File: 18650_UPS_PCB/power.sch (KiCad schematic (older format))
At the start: 37 parts, among them SW1 ENABLE, SW5 ENABLE, U2 R5478, U3 STC4054, U4 FS8205A, U5 TPS63000, U6 TPS63000

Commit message: layout almost done
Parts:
- removed JP1, JP2: PWRSAVE, Jumper:SolderJumper-3_P1.3mm_Open_RoundedPad1.0x1.5mm, symbol Jumper:SolderJumper_3_Open
- removed SW5: ENABLE, Button_Switch_THT:SW_CuK_OS102011MA1QN1_SPDT_Angled, symbol Switch:SW_SPDT
- BT1: footprint CUSTOM_FOOTPRINTS:Keystone_1042 -> Battery:BatteryHolder_Keystone_1042_1x18650
- SW1: value ENABLE -> SW_SPDT; footprint Button_Switch_THT:SW_CuK_OS102011MA1QN1_SPDT_Angled -> CUSTOM_FOOTPRINTS:ALPS_SPEF210101
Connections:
- net GNDD: no longer SW1.3 (C)
- net Shunt+: now also SW1.3 (C); no longer BT1.1 (+)
- net at U5.6 (EN): now also C6.2, R6.2, U5.8 (VINA); no longer SW1.2 (B)
- net PA4: now reaches U5.7 (PS/SYNC)
- net PA5: now reaches U6.7 (PS/SYNC)
- net at U6.6 (EN): now also C7.2, R7.2, U6.8 (VINA)
- new net: BT1.1 (+), SW1.2 (B)
- now unconnected: SW1.1 (A)
- no-connect marks 0 -> 1
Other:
- moved on the sheet: BT1
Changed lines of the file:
@@
 $Descr A4 11693 8268
 encoding utf-8
-Sheet 2 4
+Sheet 2 2
 Title ""
 Date ""
@@
 	4700 2100 4700 2200
 Connection ~ 5250 1500
-$Comp
-L Switch:SW_SPDT SW?
-U 1 1 6096E9F7
-P 5700 2000
-AR Path="/6096E9F7" Ref="SW?"  Part="1"
-AR Path="/60952D5B/6096E9F7" Ref="SW1"  Part="1"
-F 0 "SW1" H 5700 1800 50  0000 C CNN
-F 1 "ENABLE" H 5700 1700 50  0000 C CNN
-F 2 "Button_Switch_THT:SW_CuK_OS102011MA1QN1_SPDT_Angled" H 5700 2000 50  0001 C CNN
-F 3 "~" H 5700 2000 50  0001 C CNN
-	1    5700 2000
-	-1   0    0    -1
-$EndComp
-Wire Wire Line
-	5500 2100 5250 2100
-Connection ~ 5250 2100
-Wire Wire Line
-	5500 1900 5450 1900
-Wire Wire Line
-	5900 2000 5950 2000
-Wire Wire Line
-	5950 2000 5950 1600
-$Comp
-L Jumper:SolderJumper_3_Open JP?
-U 1 1 6096EA05
-P 6350 2000
-AR Path="/6096EA05" Ref="JP?"  Part="1"
-AR Path="/60952D5B/6096EA05" Ref="JP1"  Part="1"
-F 0 "JP1" H 6350 2147 50  0000 C CNN
-F 1 "PWRSAVE" H 6350 2238 50  0000 C CNN
-F 2 "Jumper:SolderJumper-3_P1.3mm_Open_RoundedPad1.0x1.5mm" H 6350 2000 50  0001 C CNN
-F 3 "~" H 6350 2000 50  0001 C CNN
-	1    6350 2000
-	-1   0    0    1
-$EndComp
-Connection ~ 5950 2000
-Wire Wire Line
-	5950 1600 6650 1600
 Wire Wire Line
 	4700 1400 6650 1400
@@
 Wire Wire Line
 	6950 2250 6950 2200
-Wire Wire Line
-	6950 2250 6650 2250
-Wire Wire Line
-	6650 2000 6650 2250
 $Comp
 L Device:C_Small C?
@@
 	4350 4650 4350 2750
 Wire Wire Line
-	6650 4100 6650 4350
-Wire Wire Line
-	6950 4350 6650 4350
-Wire Wire Line
 	6950 4350 6950 4300
 Wire Wire Line
@@
 	4700 3500 6650 3500
 Wire Wire Line
-	5950 3700 6650 3700
-$Comp
-L Jumper:SolderJumper_3_Open JP?
-U 1 1 6096EABB
-P 6350 4100
-AR Path="/6096EABB" Ref="JP?"  Part="1"
-AR Path="/60952D5B/6096EABB" Ref="JP2"  Part="1"
-F 0 "JP2" H 6350 4247 50  0000 C CNN
-F 1 "PWRSAVE" H 6350 4338 50  0000 C CNN
-F 2 "Jumper:SolderJumper-3_P1.3mm_Open_RoundedPad1.0x1.5mm" H 6350 4100 50  0001 C CNN
-F 3 "~" H 6350 4100 50  0001 C CNN
-	1    6350 4100
-	-1   0    0    1
-$EndComp
-Wire Wire Line
-	5950 4100 5950 3700
-Connection ~ 5950 4100
-Wire Wire Line
-	5900 4100 5950 4100
-Wire Wire Line
-	5450 3600 6650 3600
-Wire Wire Line
-	5450 3600 5250 3600
-Connection ~ 5450 3600
-Wire Wire Line
-	5450 4000 5450 3600
-Wire Wire Line
-	5500 4000 5450 4000
-$Comp
-L Switch:SW_SPDT SW?
-U 1 1 6096EAC9
-P 5700 4100
-AR Path="/6096EAC9" Ref="SW?"  Part="1"
-AR Path="/60952D5B/6096EAC9" Ref="SW5"  Part="1"
-F 0 "SW5" H 5700 3900 50  0000 C CNN
-F 1 "ENABLE" H 5700 3800 50  0000 C CNN
-F 2 "Button_Switch_THT:SW_CuK_OS102011MA1QN1_SPDT_Angled" H 5700 4100 50  0001 C CNN
-F 3 "~" H 5700 4100 50  0001 C CNN
-	1    5700 4100
-	-1   0    0    -1
-$EndComp
-Wire Wire Line
 	4700 4200 4700 4300
 Wire Wire Line
-	5500 4200 5250 4200
-Wire Wire Line
 	5250 4200 4700 4200
-Connection ~ 5250 4200
 Wire Wire Line
 	5250 4100 5250 4200
@@
 $EndComp
 $Comp
-L Regulator_Switching:TPS63000 U?
-U 1 1 6096EB01
-P 7050 3700
-AR Path="/6096EB01" Ref="U?"  Part="1"
-AR Path="/60952D5B/6096EB01" Ref="U6"  Part="1"
-F 0 "U6" H 6800 4300 50  0000 C CNN
-F 1 "TPS63000" H 7150 4300 50  0000 C CNN
-F 2 "Package_SON:Texas_DRC0010J_ThermalVias" H 7900 3150 50  0001 C CNN
-F 3 "http://www.ti.com/lit/ds/symlink/tps63000.pdf" H 6750 4250 50  0001 C CNN
-	1    7050 3700
-	1    0    0    -1
-$EndComp
-$Comp
 L power:GNDD #PWR?
 U 1 1 6096EB07
@@
 Text Notes 800  850  0    50   ~ 0
 CC/CV Charger
-Wire Notes Line
-	650  4850 650  6750
-Wire Notes Line
-	2250 6750 650  6750
-Wire Notes Line
-	2250 4850 2250 6750
-Wire Notes Line
-	650  4850 2250 4850
-Wire Wire Line
-	1500 6350 1500 6400
-Connection ~ 1500 6350
-Wire Wire Line
-	1700 6350 1500 6350
-Wire Wire Line
-	1700 6400 1700 6350
+Wire Wire Line
+	1500 7000 1500 7050
+Connection ~ 1500 7000
+Wire Wire Line
+	1700 7000 1500 7000
+Wire Wire Line
+	1700 7050 1700 7000
 $Comp
 L power:GND #PWR?
 U 1 1 6097A865
-P 1700 6400
+P 1700 7050
 AR Path="/6097A865" Ref="#PWR?"  Part="1"
 AR Path="/60952D5B/6097A865" Ref="#PWR010"  Part="1"
-F 0 "#PWR010" H 1700 6150 50  0001 C CNN
-F 1 "GND" H 1705 6227 50  0000 C CNN
-F 2 "" H 1700 6400 50  0001 C CNN
-F 3 "" H 1700 6400 50  0001 C CNN
-	1    1700 6400
-	1    0    0    -1
-$EndComp
-Wire Wire Line
-	1500 6300 1500 6350
+F 0 "#PWR010" H 1700 6800 50  0001 C CNN
+F 1 "GND" H 1705 6877 50  0000 C CNN
+F 2 "" H 1700 7050 50  0001 C CNN
+F 3 "" H 1700 7050 50  0001 C CNN
+	1    1700 7050
+	1    0    0    -1
+$EndComp
+Wire Wire Line
+	1500 6950 1500 7000
 $Comp
 L power:-BATT #PWR?
 U 1 1 6097A86D
-P 1500 6400
+P 1500 7050
 AR Path="/6097A86D" Ref="#PWR?"  Part="1"
 AR Path="/60952D5B/6097A86D" Ref="#PWR09"  Part="1"
-F 0 "#PWR09" H 1500 6250 50  0001 C CNN
-F 1 "-BATT" H 1515 6573 50  0000 C CNN
-F 2 "" H 1500 6400 50  0001 C CNN
-F 3 "" H 1500 6400 50  0001 C CNN
-	1    1500 6400
+F 0 "#PWR09" H 1500 6900 50  0001 C CNN
+F 1 "-BATT" H 1515 7223 50  0000 C CNN
+F 2 "" H 1500 7050 50  0001 C CNN
+F 3 "" H 1500 7050 50  0001 C CNN
+	1    1500 7050
 	-1   0    0    1
 $EndComp
@@
 L Device:Battery_Cell BT?
 U 1 1 6097A87A
-P 1500 6200
+P 1500 6850
 AR Path="/6097A87A" Ref="BT?"  Part="1"
 AR Path="/60952D5B/6097A87A" Ref="BT1"  Part="1"
-F 0 "BT1" H 1100 6300 50  0000 L CNN
-F 1 "INR18650-35E" H 800 6200 50  0000 L CNN
-F 2 "CUSTOM_FOOTPRINTS:Keystone_1042" V 1500 6260 50  0001 C CNN
-F 3 "~" V 1500 6260 50  0001 C CNN
-	1    1500 6200
+F 0 "BT1" H 1100 6950 50  0000 L CNN
+F 1 "INR18650-35E" H 800 6850 50  0000 L CNN
+F 2 "Battery:BatteryHolder_Keystone_1042_1x18650" V 1500 6910 50  0001 C CNN
+F 3 "~" V 1500 6910 50  0001 C CNN
+	1    1500 6850
 	1    0    0    -1
 $EndComp
@@
 	1    0    0    -1
 $EndComp
-Wire Wire Line
-	5450 1500 6650 1500
-Wire Wire Line
-	5450 1500 5250 1500
-Connection ~ 5450 1500
-Wire Wire Line
-	5450 1900 5450 1500
 $Comp
 L Device:C_Small C?
@@
 Wire Notes Line
 	4350 2550 9950 2550
-Wire Wire Line
-	6550 4100 6650 4100
-Wire Wire Line
-	5950 4100 6150 4100
-Wire Wire Line
-	6350 3950 6350 3900
-Wire Wire Line
-	6350 3900 6650 3900
 $Comp
 L Device:R R2
@@
 Wire Wire Line
 	1600 5900 1500 5900
-Connection ~ 1500 5900
-Wire Wire Line
-	1500 5900 1500 6000
+Wire Wire Line
+	1500 6550 1500 6650
 Wire Wire Line
 	1600 5500 1500 5500
@@
 Wire Wire Line
 	1500 5500 1500 5550
-Wire Wire Line
-	6550 2000 6650 2000
-Wire Wire Line
-	5950 2000 6150 2000
-Wire Wire Line
-	6350 1850 6350 1800
-Wire Wire Line
-	6350 1800 6650 1800
 $Comp
 L power:GNDD #PWR?
@@
 	1    0    0    -1
 $EndComp
+Text GLabel 6550 3900 0    50   Input ~ 0
+PA5
+Wire Wire Line
+	5250 3600 6400 3600
+$Comp
+L Regulator_Switching:TPS63000 U?
+U 1 1 6096EB01
+P 7050 3700
+AR Path="/6096EB01" Ref="U?"  Part="1"
+AR Path="/60952D5B/6096EB01" Ref="U6"  Part="1"
+F 0 "U6" H 6800 4300 50  0000 C CNN
+F 1 "TPS63000" H 7150 4300 50  0000 C CNN
+F 2 "Package_SON:Texas_DRC0010J_ThermalVias" H 7900 3150 50  0001 C CNN
+F 3 "http://www.ti.com/lit/ds/symlink/tps63000.pdf" H 6750 4250 50  0001 C CNN
+	1    7050 3700
+	1    0    0    -1
+$EndComp
+Wire Wire Line
+	6650 3900 6550 3900
+Wire Wire Line
+	5250 1500 6400 1500
+Text GLabel 6500 1800 0    50   Input ~ 0
+PA4
+Wire Wire Line
+	6500 1800 6650 1800
+Wire Wire Line
+	6400 1600 6400 1500
+Wire Wire Line
+	6400 1600 6650 1600
+Connection ~ 6400 1500
+Wire Wire Line
+	6400 1500 6650 1500
+Wire Notes Line
+	650  4850 650  7600
+Wire Notes Line
+	650  7600 2300 7600
+Wire Notes Line
+	2300 4850 2300 7600
+Wire Notes Line
+	650  4850 2300 4850
+Wire Wire Line
+	6400 3700 6400 3600
+Wire Wire Line
+	6400 3700 6650 3700
+Connection ~ 6400 3600
+Wire Wire Line
+	6400 3600 6650 3600
+$Comp
+L Switch:SW_SPDT SW1
+U 1 1 60BDD630
+P 1500 6350
+F 0 "SW1" V 1546 6162 50  0000 R CNN
+F 1 "SW_SPDT" V 1455 6162 50  0000 R CNN
+F 2 "CUSTOM_FOOTPRINTS:ALPS_SPEF210101" H 1500 6350 50  0001 C CNN
+F 3 "~" H 1500 6350 50  0001 C CNN
+	1    1500 6350
+	0    -1   -1   0
+$EndComp
+Wire Wire Line
+	1600 6150 1600 6000
+Wire Wire Line
+	1600 6000 1500 6000
+Wire Wire Line
+	1500 6000 1500 5900
+Connection ~ 1500 5900
+NoConn ~ 1400 6150
 $EndSCHEMATC

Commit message: routing done
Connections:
- net at C7.2, R7.2, U6.8 (VINA): no longer U6.6 (EN)
- new net PA6: U6.6 (EN)
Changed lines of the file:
@@
 Text GLabel 6550 3900 0    50   Input ~ 0
 PA5
-Wire Wire Line
-	5250 3600 6400 3600
 $Comp
 L Regulator_Switching:TPS63000 U?
@@
 Wire Notes Line
 	650  4850 2300 4850
-Wire Wire Line
-	6400 3700 6400 3600
-Wire Wire Line
-	6400 3700 6650 3700
-Connection ~ 6400 3600
-Wire Wire Line
-	6400 3600 6650 3600
 $Comp
 L Switch:SW_SPDT SW1
@@
 Connection ~ 1500 5900
 NoConn ~ 1400 6150
+Text GLabel 6550 3700 0    50   Input ~ 0
+PA6
+Wire Wire Line
+	5250 3600 6650 3600
+Wire Wire Line
+	6550 3700 6650 3700
 $EndSCHEMATC

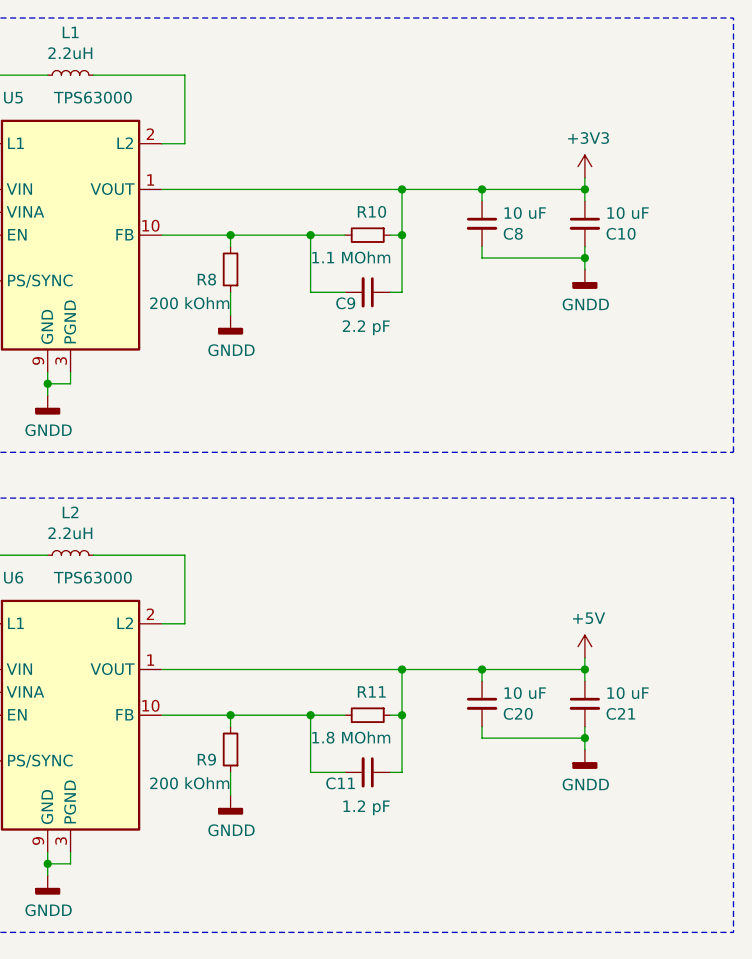
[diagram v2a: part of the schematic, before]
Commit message: changed resistor values tps63000
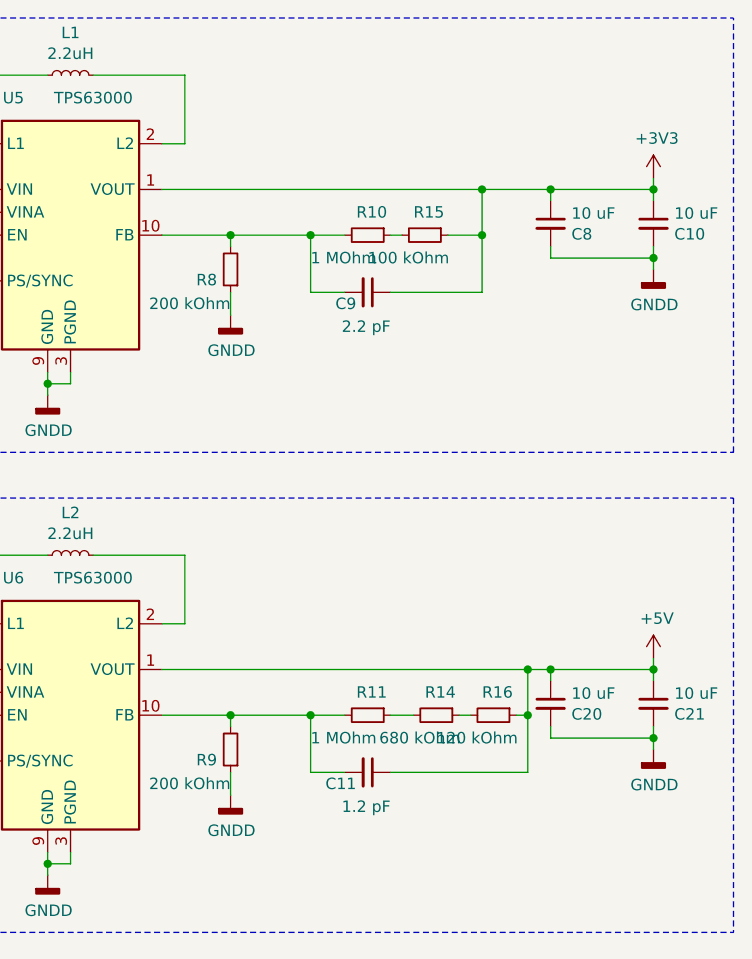
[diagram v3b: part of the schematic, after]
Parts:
- added R14: 680 kOhm, Resistor_SMD:R_0603_1608Metric, symbol Device:R_Small
- added R15: 100 kOhm, Resistor_SMD:R_0603_1608Metric, symbol Device:R_Small
- added R16: 120 kOhm, Resistor_SMD:R_0603_1608Metric, symbol Device:R_Small
- R10: value 1.1 MOhm -> 1 MOhm
- R11: value 1.8 MOhm -> 1 MOhm
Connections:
- net +3V3: now also R15.1; no longer R10.1
- net +5V: now also R16.1; no longer R11.1
- new net: R10.1, R15.2
- new net: R14.1, R16.2
- new net: R11.1, R14.2
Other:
- moved on the sheet: C10, C20, C21, C8

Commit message: ordered
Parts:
- U3: footprint Package_TO_SOT_SMD:TSOT-23-5_HandSoldering -> Package_TO_SOT_SMD:TSOT-23-5
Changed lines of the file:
@@
 F 0 "U3" H 2925 1665 50  0000 C CNN
 F 1 "STC4054" H 2925 1574 50  0000 C CNN
-F 2 "Package_TO_SOT_SMD:TSOT-23-5_HandSoldering" H 2600 2100 50  0001 C CNN
+F 2 "Package_TO_SOT_SMD:TSOT-23-5" H 2600 2100 50  0001 C CNN
 F 3 "" H 2850 1550 50  0001 C CNN
 	1    2650 1400
